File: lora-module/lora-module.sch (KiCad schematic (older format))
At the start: 28 parts, among them J1 North, J2 South, J3 West, J4 East, J5 Conn_Coaxial, U3 BA033CC0FP-E2, U4 MAX3486, U5 MAX3486, U7 RFM95W-868S2

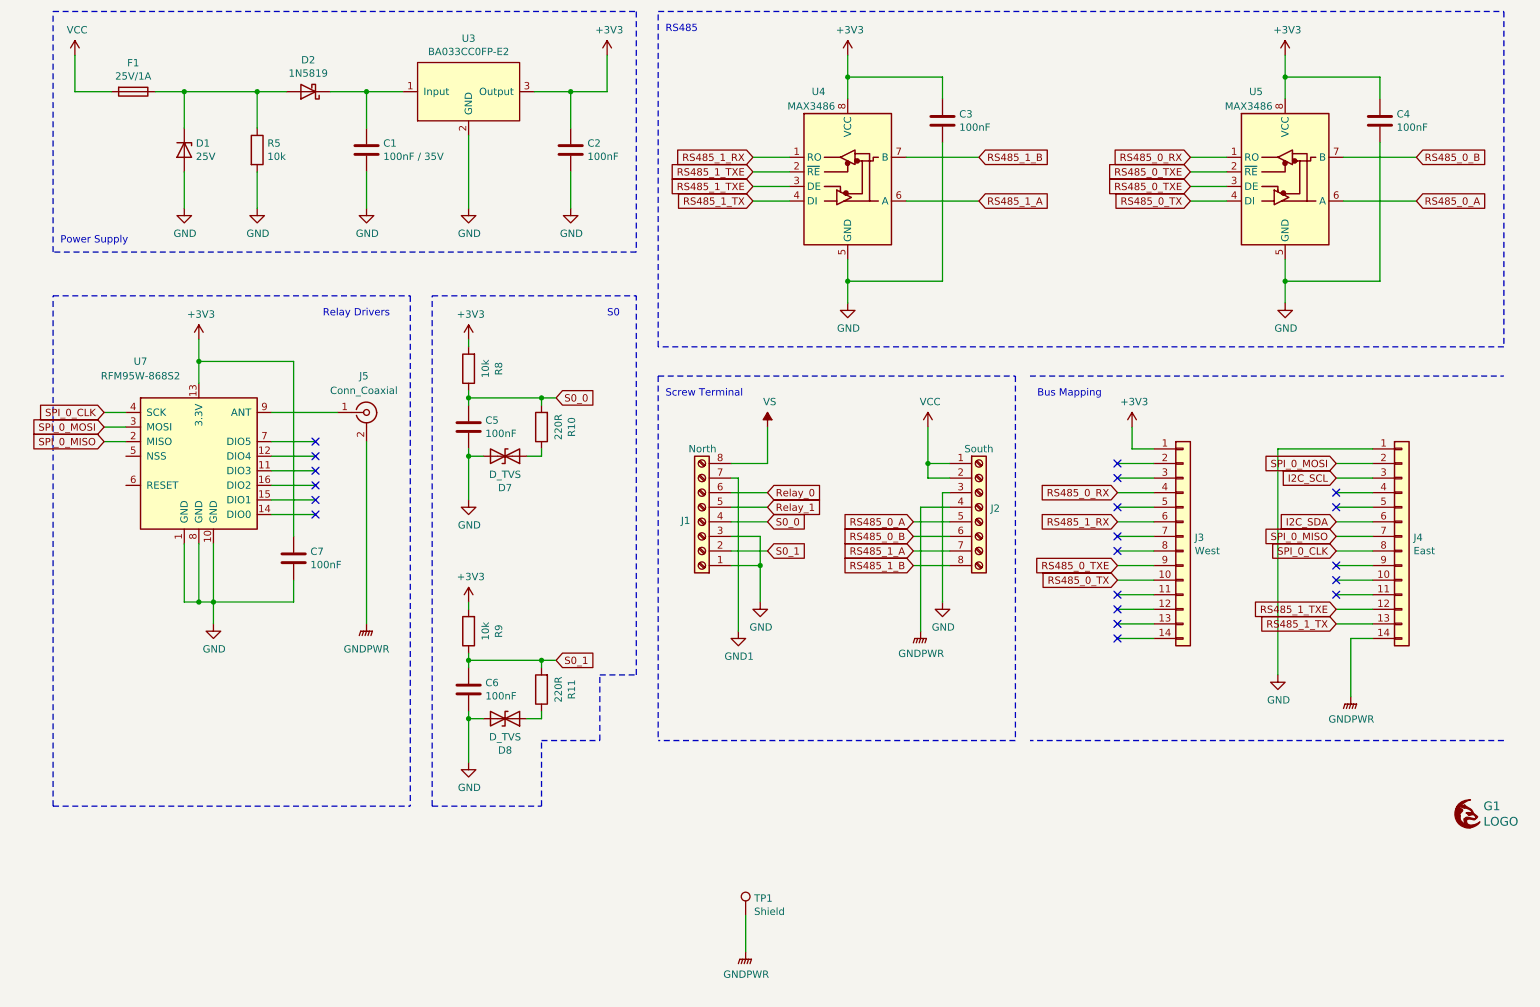
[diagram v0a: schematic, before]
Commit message: Added SMA connector for LoRa module
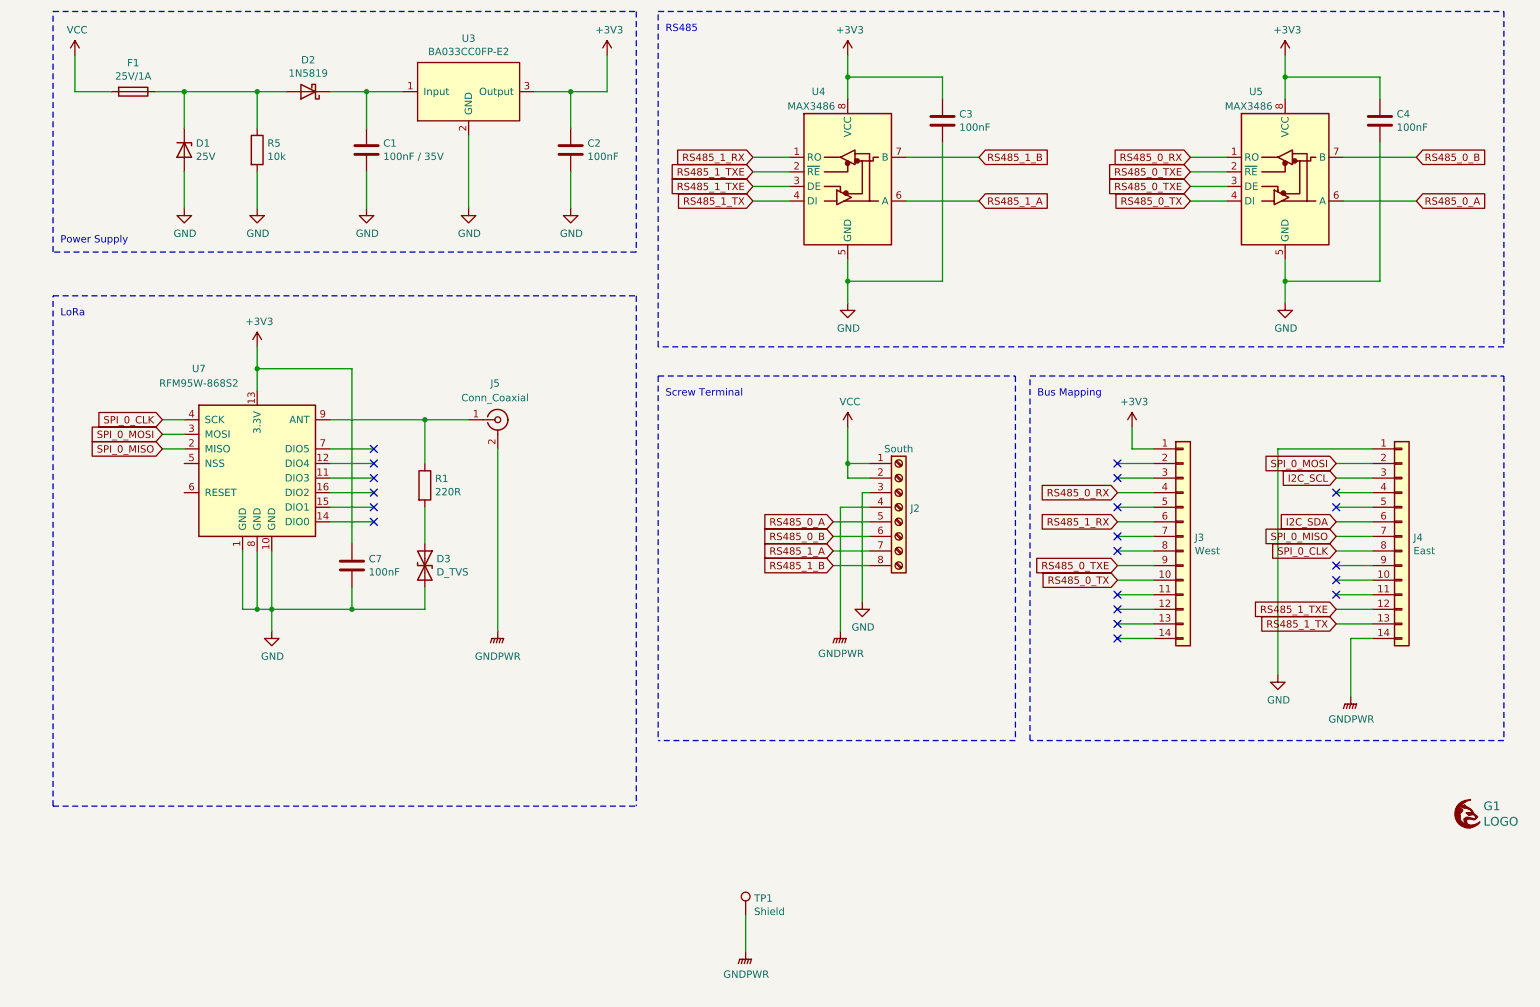
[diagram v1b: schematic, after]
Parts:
- removed C5, C6: 100nF, Capacitor_SMD:C_1206_3216Metric_Pad1.33x1.80mm_HandSolder, symbol Device:C
- removed D7, D8: D_TVS, Diode_SMD:D_0603_1608Metric_Pad1.05x0.95mm_HandSolder, symbol Device:D_TVS
- removed J1: North, footprints:PHOENIX_1727078, symbol Connector:Screw_Terminal_01x08
- removed R10, R11: 220R, Resistor_SMD:R_1206_3216Metric_Pad1.30x1.75mm_HandSolder, symbol Device:R
- removed R8, R9: 10k, Resistor_SMD:R_1206_3216Metric_Pad1.30x1.75mm_HandSolder, symbol Device:R
- added D3: D_TVS, symbol Device:D_TVS
- added R1: 220R, Resistor_SMD:R_1206_3216Metric_Pad1.30x1.75mm_HandSolder, symbol Device:R
- J5: footprint Connector_Coaxial:SMA_Molex_73251-2200_Horizontal -> footprints:LINX_CONSMA002
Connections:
- net GND: now also D3.2 (A2)
- net at J5.1 (In), U7.9 (ANT): now also R1.1
- new net: D3.1 (A1), R1.2
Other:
- note added: "LoRa"
- note removed: "Relay Drivers"
- note removed: "S0"
- moved on the sheet: C7, J2, J5, U7

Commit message: Ongoing work LoRa module
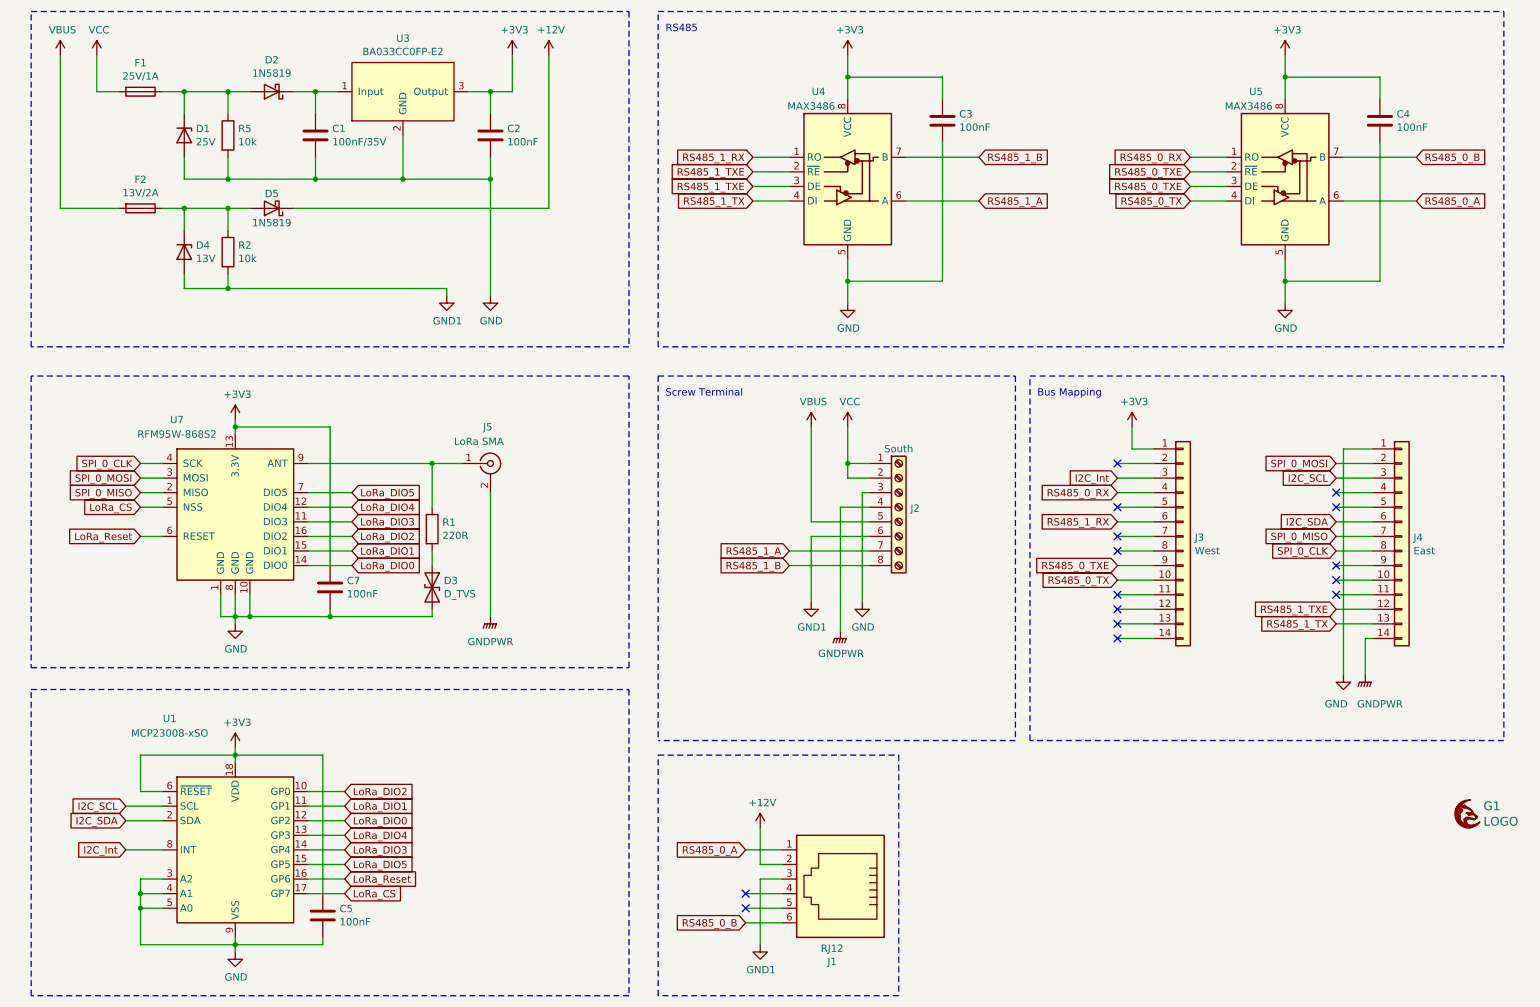
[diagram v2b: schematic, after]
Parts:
- removed TP1: Shield, TestPoint:TestPoint_Pad_D4.0mm, symbol Connector:TestPoint
- added C5: 100nF, Capacitor_SMD:C_1206_3216Metric_Pad1.33x1.80mm_HandSolder, symbol Device:C
- added D4: 13V, Diode_SMD:D_SOD-523, symbol Device:D_Zener
- added D5: 1N5819, Diode_SMD:D_SOD-323_HandSoldering, symbol Diode:1N5819
- added F2: 13V/2A, Fuse:Fuse_1206_3216Metric_Pad1.42x1.75mm_HandSolder, symbol Device:Fuse
- added J1: RJ12, footprints:Molex-95501-6669-MFG, symbol Connector:RJ12
- added R2: 10k, Resistor_SMD:R_1206_3216Metric_Pad1.30x1.75mm_HandSolder, symbol Device:R
- added U1: MCP23008-xSO, Package_SO:SOIC-18W_7.5x11.6mm_P1.27mm, symbol Interface_Expansion:MCP23008-xSO
- C1: value 100nF / 35V -> 100nF/35V
- D3: footprint (none) -> Diode_SMD:D_0603_1608Metric_Pad1.05x0.95mm_HandSolder; Price (none) -> 0.32; Product (none) -> https://www.mouser.de/ProductDetail/Bourns/CG0603MLC-33LE?q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
- G1: Price (none) -> N/A; Product (none) -> N/A
- J5: value Conn_Coaxial -> LoRa SMA
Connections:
- net +3V3: now also C5.1, U1.18 (VDD), U1.6 (~RESET)
- net GND: now also C5.2, U1.3 (A2), U1.4 (A1), U1.5 (A0), U1.9 (VSS)
- net I2C_SCL: now also U1.1 (SCL)
- net I2C_SDA: now also U1.2 (SDA)
- net RS485_0_A: now also J1.1; no longer J2.5 (Pin_5)
- net RS485_0_B: now also J1.6; no longer J2.6 (Pin_6)
- net I2C_Int: now reaches J3.3 (Pin_3)
- net I2C_Int: now also U1.8 (INT)
- net LoRa_DIO3: now reaches U7.11 (DIO3)
- net LoRa_DIO3: now also U1.14 (GP4)
- net LoRa_DIO4: now reaches U7.12 (DIO4)
- net LoRa_DIO4: now also U1.13 (GP3)
- net LoRa_DIO0: now reaches U7.14 (DIO0)
- net LoRa_DIO0: now also U1.12 (GP2)
- net LoRa_DIO1: now reaches U7.15 (DIO1)
- net LoRa_DIO1: now also U1.11 (GP1)
- net LoRa_DIO2: now reaches U7.16 (DIO2)
- net LoRa_DIO2: now also U1.10 (GP0)
- net LoRa_CS: now reaches U7.5 (NSS)
- net LoRa_CS: now also U1.17 (GP7)
- net LoRa_Reset: now reaches U7.6 (RESET)
- net LoRa_Reset: now also U1.16 (GP6)
- net LoRa_DIO5: now reaches U7.7 (DIO5)
- net LoRa_DIO5: now also U1.15 (GP5)
- new net: D4.1 (K), D5.2 (A), F2.1, R2.1
- new net +12V: D5.1 (K), J1.2
- new net GND1: D4.2 (A), J1.3, J2.6 (Pin_6), R2.2
- new net VBUS: F2.2, J2.5 (Pin_5)
- no-connect marks 20 -> 15
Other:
- note removed: "LoRa"
- note removed: "Power Supply"
- moved on the sheet: C1, C2, C7, D1, D2, D3, F1, J5, R1, R5, U3, U7

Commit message: Added OpenHardware Logo to PCBs
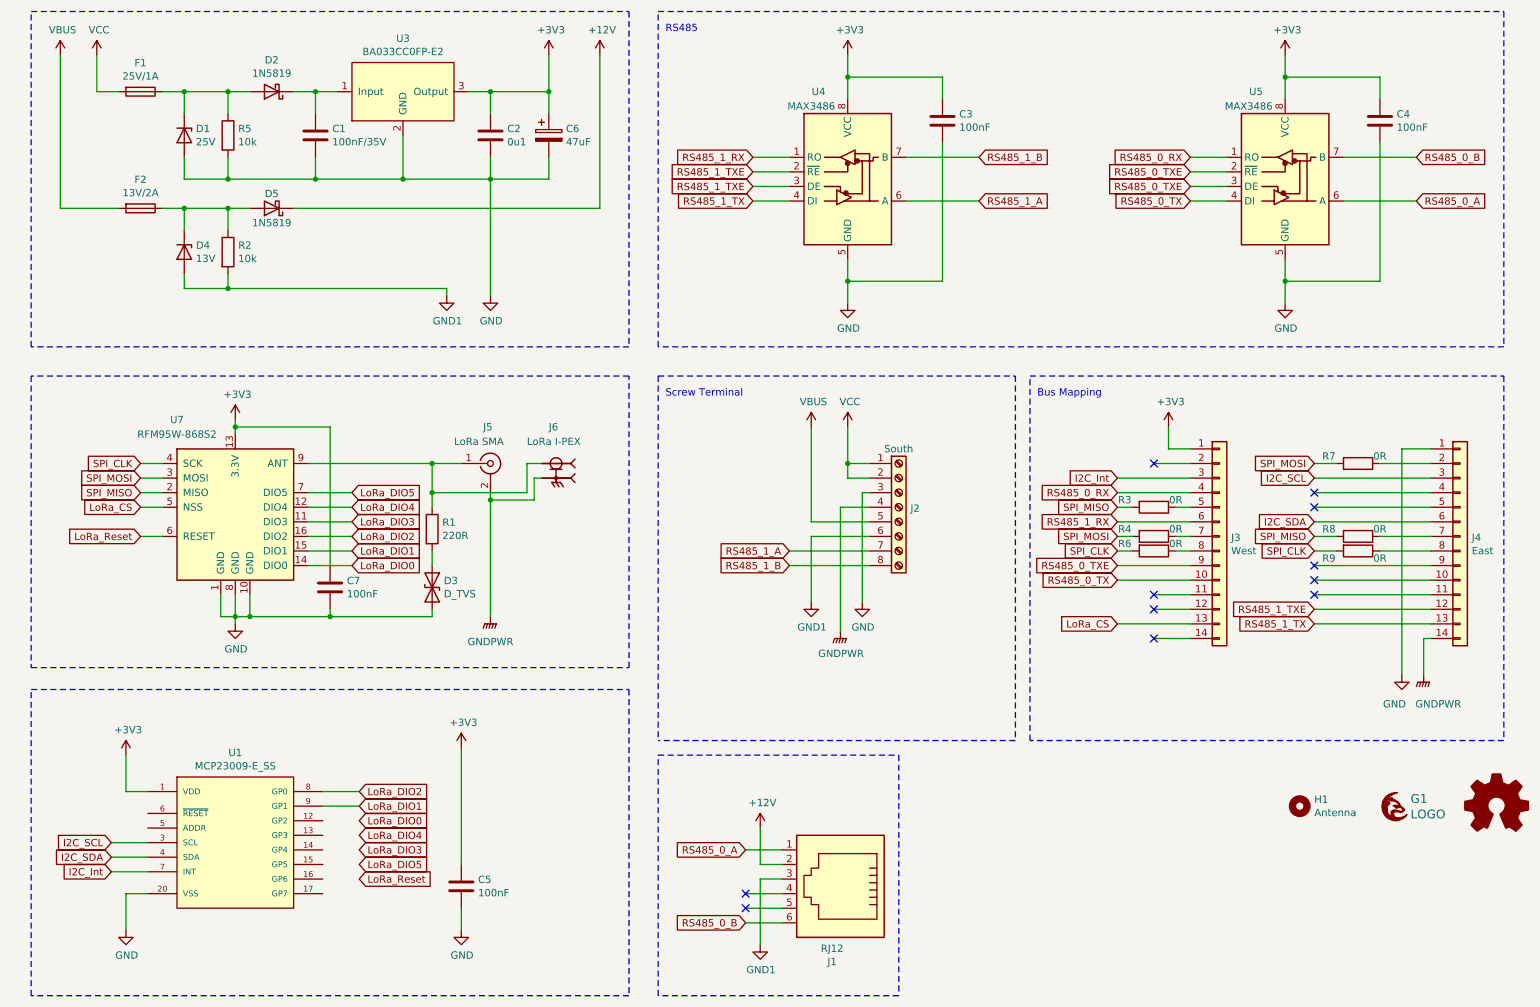
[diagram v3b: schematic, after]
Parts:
- removed U1: MCP23008-xSO, Package_SO:SOIC-18W_7.5x11.6mm_P1.27mm, symbol Interface_Expansion:MCP23008-xSO
- added C6: 47uF, Capacitor_SMD:CP_Elec_5x5.3, symbol Device:CP
- added G2: Logo_Open_Hardware_Small, Symbol:OSHW-Logo2_7.3x6mm_SilkScreen, symbol Graphic:Logo_Open_Hardware_Small
- added H1: Antenna, MountingHole:MountingHole_3.7mm, symbol Mechanical:MountingHole
- added J6: LoRa I-PEX, SAMTEC_RSP-122811-01, symbol RSP-122811-01:RSP-122811-01
- added R3, R4, R6, R7, R8, R9: 0R, Resistor_SMD:R_1206_3216Metric_Pad1.30x1.75mm_HandSolder, symbol Device:R
- added U1: MCP23009-E_SS, SOP65P780X200-20N, symbol MCP23009-E_SS:MCP23009-E_SS
- C2: value 100nF -> 0u1
- G1: Price N/A -> 0
- J1: footprint footprints:Molex-95501-6669-MFG -> footprints:CUI_CRJ030-G-TH; Price (none) -> 1.32; Product (none) -> https://www.mouser.de/ProductDetail/CUI-Devices/CRJ030-G-TH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
- J3, J4: Price 0.45 -> 0; Product https://www.mouser.de/ProductDetail/Harwin/M20-9991446 -> N/A
- J5: Price (none) -> 4.35; Product (none) -> https://www.mouser.de/ProductDetail/Linx-Technologies/CONSM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
- U7: Price (none) -> 18.75; Product (none) -> https://www.mouser.de/ProductDetail/RF-Solutions/RFM95W-868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
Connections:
- net +3V3: now also C6.1, U1.1 (VDD)
- net GND: now also C6.2, U1.20 (VSS)
- net GNDPWR: now also J6.G1, J6.G2
- net I2C_Int: now also U1.7 (INT)
- net I2C_SCL: now also U1.3 (SCL)
- net I2C_SDA: now also U1.4 (SDA)
- net LoRa_CS: now also J3.13 (Pin_13)
- net LoRa_DIO1: now also U1.9 (GP1)
- net LoRa_DIO2: now also U1.8 (GP0)
- net at J3.5 (Pin_5): now also R3.1
- net at J3.7 (Pin_7): now also R4.1
- net at J3.8 (Pin_8): now also R6.1
- net at J5.1 (In), R1.1, U7.9 (ANT): now also J6.1
- net SPI_0_CLK: no longer names the net of J4.8 (Pin_8)
- net SPI_0_CLK: now also R9.1; no longer U7.4 (SCK)
- net SPI_0_MISO: no longer names the net of J4.7 (Pin_7)
- net SPI_0_MISO: now also R8.1; no longer U7.2 (MISO)
- net SPI_0_MOSI: no longer names the net of J4.2 (Pin_2)
- net SPI_0_MOSI: now also R7.1; no longer U7.3 (MOSI)
- new net SPI_CLK: R6.2, R9.2, U7.4 (SCK)
- new net SPI_MISO: R3.2, R8.2, U7.2 (MISO)
- new net SPI_MOSI: R4.2, R7.2, U7.3 (MOSI)
- no-connect marks 15 -> 11
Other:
- moved on the sheet: C5, G1, J3, J4
